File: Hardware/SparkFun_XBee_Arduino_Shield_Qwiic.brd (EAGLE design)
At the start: 53.3 x 59.7 mm, 172 parts, among them J4 QWIIC_RIGHT_ANGLE, Q1 3.1A/30V/105mΩ, Q2 3.1A/30V/105mΩ, Q3 3.1A/30V/105mΩ, Q4 5.8A/30V/35mΩ, Q5 20V/4.2A/52mΩ/1.4W, U1 FSUSB30MUX_MSOP10, U2 AP63203, U3 ESD Diode, U4 FT231XS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

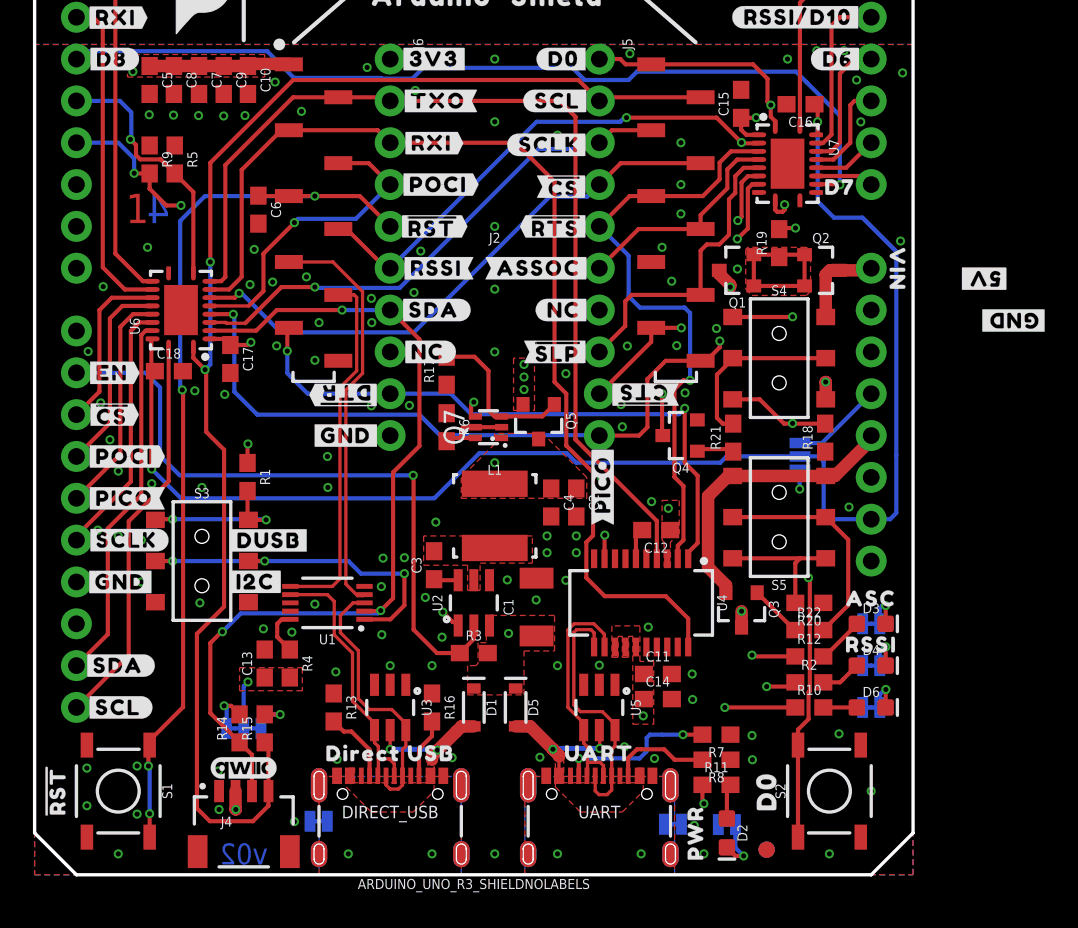
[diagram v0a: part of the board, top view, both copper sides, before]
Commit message: Adds silk
* Adds enable net, needs route
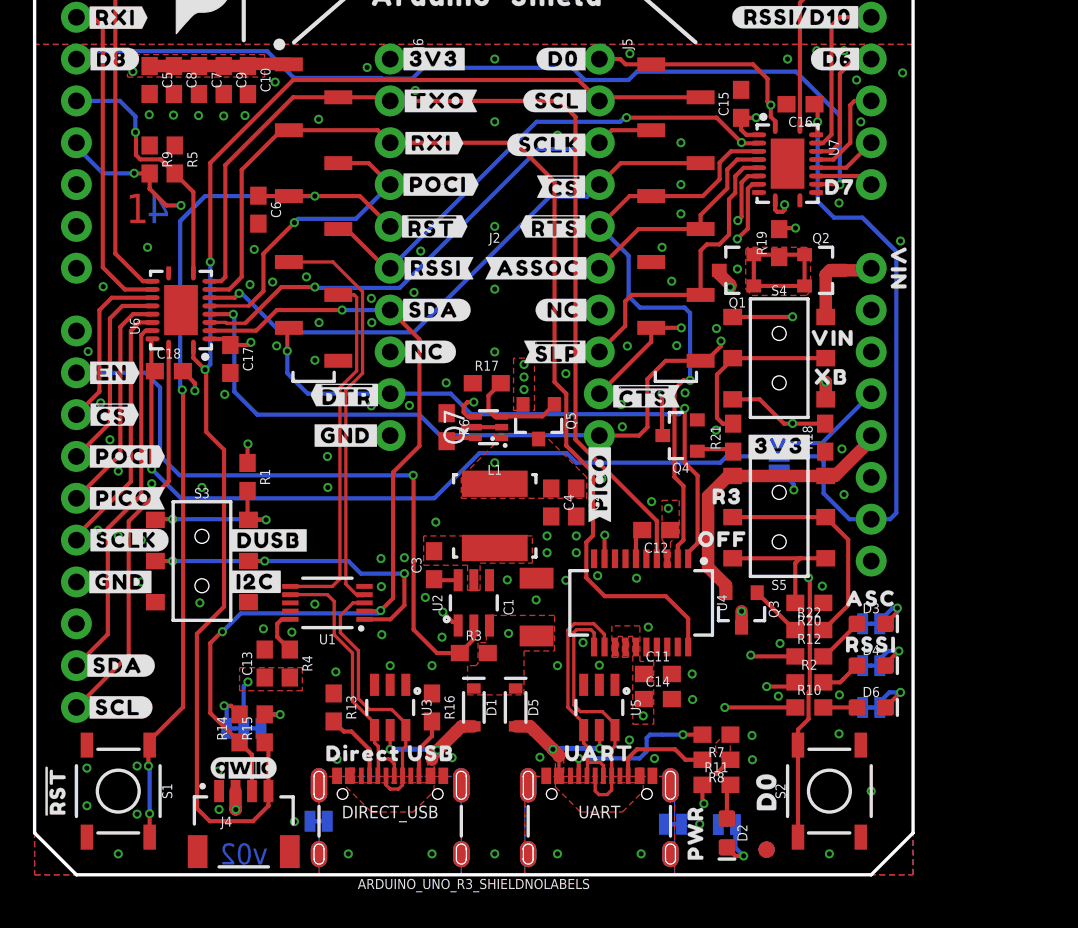
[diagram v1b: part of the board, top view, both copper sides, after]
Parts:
- added U$12: (no value), top:##CTS##28
- added U$41: (no value), topmirror:#GND#0
- added U$44: (no value), top:#3V3#1
- added U$8: (no value), topmirror:##DTR##27
- added U$87: (no value), pot:XB9
- U$31: device topmirror:##CTS##26 -> top:#PICO#26
- U$67: device topmirror:#3V3#2 -> pot:R310
- U$69: device top:##DTR##27 -> pot:OFF311
- U$70: device top:#PICO#24 -> pot:VIN8
- moved U$69 24.5 mm to (41.8, 20.4), turned to 0 degrees
- moved U$70 16.6 mm to (48.5, 32.6), turned to 0 degrees
- moved U$67 16.4 mm to (42.1, 23.0), flipped to the top, turned to 0 degrees
- moved U$29 11.5 mm to (48.1, 31.7), flipped to the bottom, turned to 0 degrees
- moved U$39 11.4 mm to (48.6, 29.2), flipped to the bottom, turned to 0 degrees
- moved U$31 5.92 mm to (34.3, 23.9), turned to 90 degrees
- moved R17 2.55 mm to (27.5, 29.8), turned to 0 degrees
- moved U$89 2.40 mm to (47.0, 25.5)
- moved JP3 1.27 mm to (45.2, 25.4)
- moved U$66 0.08 mm to (52.5, 36.8)
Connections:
- net N$16 renamed OFF_3V3
- net N$24 renamed OFF_VIN
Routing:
- net N$20: track 9.76 -> 6.41 mm
- net GND: track 1.90 -> 4.61 mm, vias 113 -> 123
- net 5V: track 5.56 -> 6.83 mm
- net 3.3V: track 23.9 -> 25.0 mm
- net 3.3V_VREG: track 11.8 -> 12.7 mm
- net N$17: track 2.38 -> 3.12 mm
- net VIN: track 40.0 -> 39.3 mm
- net IOREF: track 87.8 -> 87.3 mm
- net D8/!DTR!: track 54.1 -> 53.6 mm

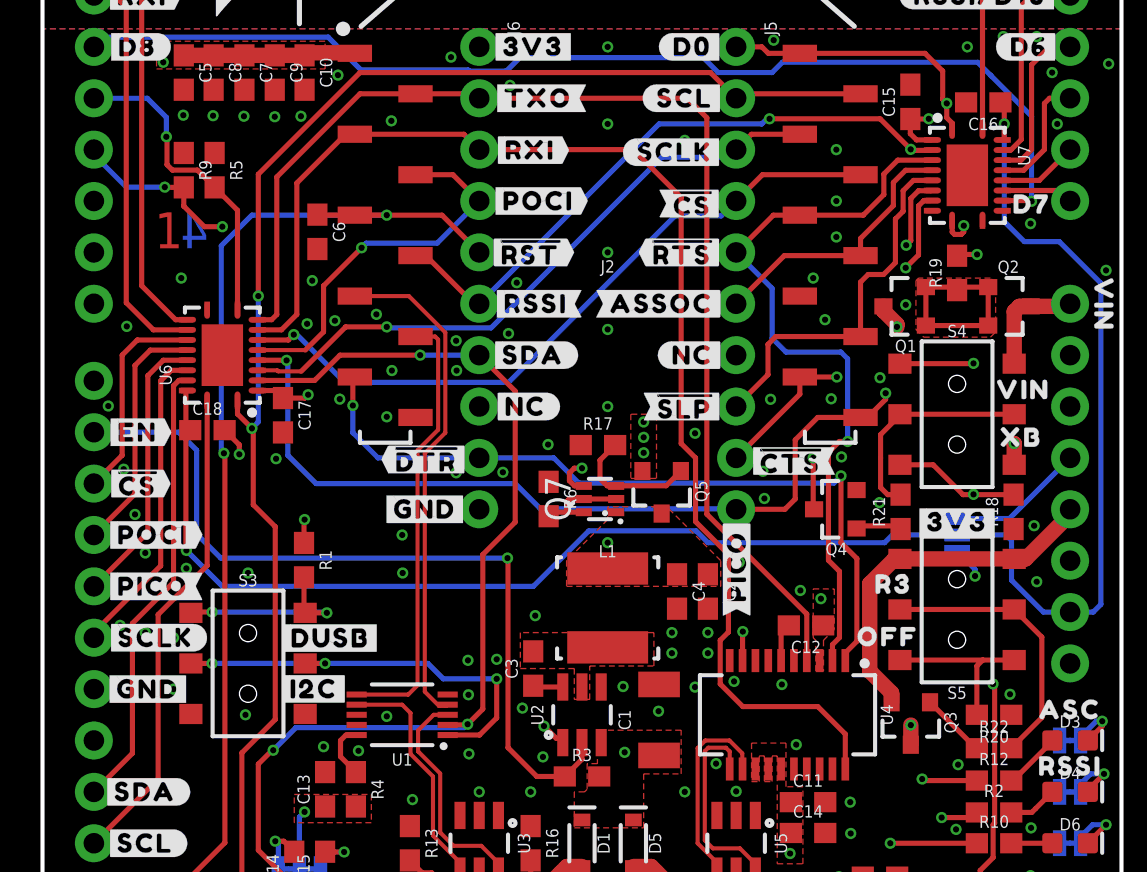
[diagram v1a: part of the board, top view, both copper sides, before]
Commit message: Routes enable pin
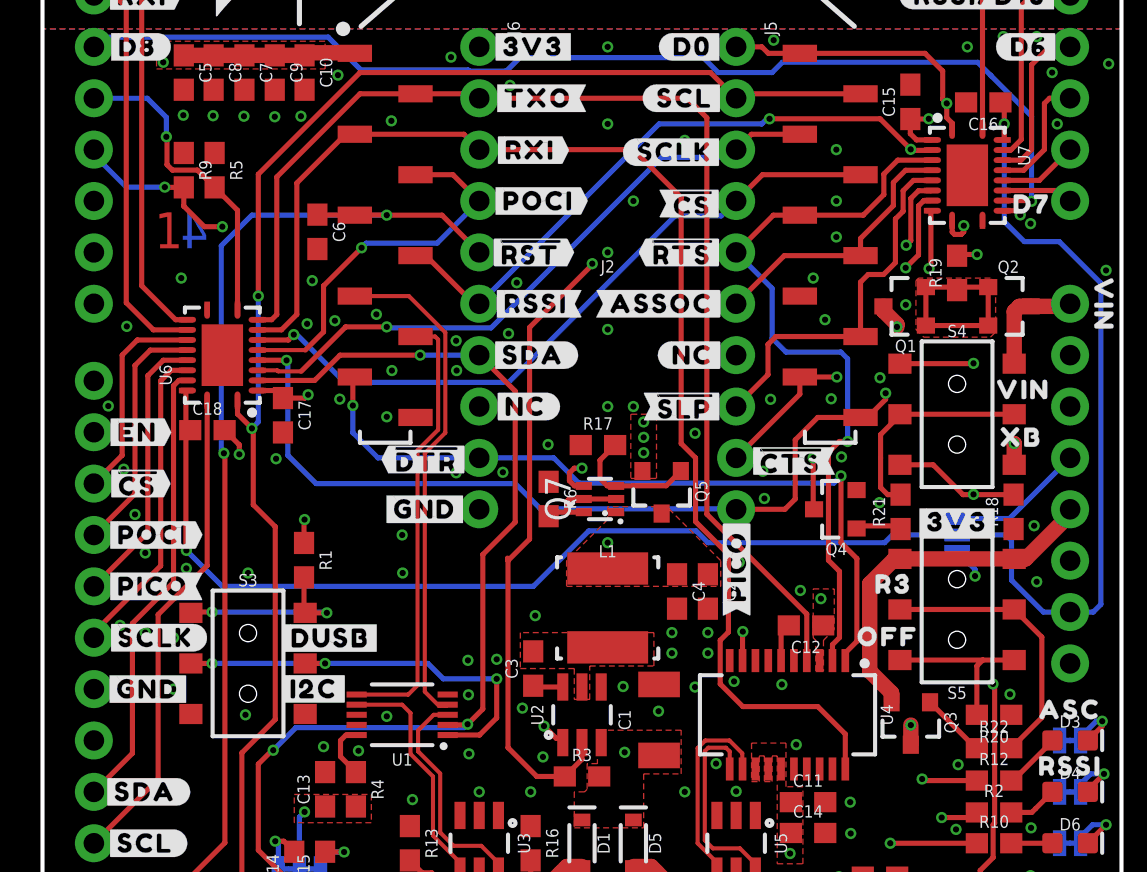
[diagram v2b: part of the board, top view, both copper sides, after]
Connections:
- new net EN_TRANS: B1.D9, U7.12
- net EN: now also U7.9; no longer B1.D9
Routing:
- net EN_TRANS: track 0.00 -> 57.7 mm, vias 0 -> 3
- net EN: track 40.3 -> 51.3 mm, vias 1 -> 2
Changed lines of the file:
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@@
 <wire x1="26.67" y1="14.312" x2="25.82" y2="13.462" width="0.254" layer="1"/>
 <wire x1="25.82" y1="13.462" x2="24.4348" y2="13.462" width="0.254" layer="1"/>
-<wire x1="23.0124" y1="24.2316" x2="23.0124" y2="14.8844" width="0.254" layer="1"/>
+<wire x1="23.0124" y1="24.2316" x2="23.0124" y2="24.13" width="0.254" layer="1"/>
+<wire x1="23.0124" y1="24.13" x2="23.0124" y2="14.8844" width="0.254" layer="1"/>
 <wire x1="24.4348" y1="13.462" x2="23.0124" y2="14.8844" width="0.254" layer="1"/>
 <wire x1="23.0124" y1="24.2316" x2="22.987" y2="24.257" width="0.254" layer="1"/>
-<via x="22.987" y="24.257" extent="1-16" drill="0.3048"/>
-<wire x1="22.987" y1="24.257" x2="8.8138" y2="24.257" width="0.254" layer="16"/>
-<wire x1="8.8138" y1="24.257" x2="7.62" y2="25.4508" width="0.254" layer="16"/>
-<contactref element="B1" pad="D9"/>
-<wire x1="7.62" y1="25.4508" x2="7.62" y2="29.591" width="0.254" layer="16"/>
-<wire x1="7.62" y1="29.591" x2="6.731" y2="30.48" width="0.254" layer="16"/>
-<wire x1="6.731" y1="30.48" x2="2.54" y2="30.48" width="0.254" layer="16"/>
+<contactref element="U7" pad="9"/>
+<wire x1="23.0124" y1="24.13" x2="24.0792" y2="25.1968" width="0.254" layer="1"/>
+<wire x1="24.0792" y1="35.6616" x2="27.2034" y2="38.7858" width="0.254" layer="1"/>
+<wire x1="27.2034" y1="38.7858" x2="27.178" y2="38.8112" width="0.254" layer="1"/>
+<via x="27.178" y="38.8112" extent="1-16" drill="0.3048"/>
+<wire x1="24.0792" y1="25.1968" x2="24.0792" y2="35.6616" width="0.254" layer="1"/>
+<wire x1="27.178" y1="38.8112" x2="32.5882" y2="38.8112" width="0.254" layer="15"/>
+<wire x1="32.5882" y1="38.8112" x2="33.2486" y2="38.1508" width="0.254" layer="15"/>
+<wire x1="33.2486" y1="38.1508" x2="43.434" y2="38.1508" width="0.254" layer="15"/>
+<wire x1="43.434" y1="38.1508" x2="43.8404" y2="38.5572" width="0.254" layer="15"/>
+<wire x1="43.8404" y1="38.5572" x2="43.8277" y2="38.5699" width="0.254" layer="15"/>
+<via x="43.8277" y="38.5699" extent="1-16" drill="0.3048"/>
+<wire x1="43.92" y1="41.43" x2="43.92" y2="38.6622" width="0.254" layer="1"/>
+<wire x1="43.92" y1="38.6622" x2="43.8277" y2="38.5699" width="0.254" layer="1"/>
 </signal>
 <signal name="N$2">
@@
 <wire x1="50.2666" y1="39.9034" x2="48.5394" y2="39.9034" width="0.254" layer="16"/>
 <wire x1="48.5394" y1="39.9034" x2="47.5454" y2="40.8974" width="0.254" layer="16"/>
-<wire x1="47.5454" y1="40.8974" x2="47.5454" y2="45.72" width="0.254" layer="16"/>
+<wire x1="47.5454" y1="40.8974" x2="47.5454" y2="41.91" width="0.254" layer="16"/>
 <via x="47.5454" y="45.72" extent="1-16" drill="0.3048"/>
+<wire x1="47.5454" y1="41.91" x2="47.5454" y2="45.72" width="0.254" layer="16"/>
 <wire x1="52.324" y1="37.846" x2="50.2666" y2="39.9034" width="0.254" layer="16"/>
 </signal>
@@
 <wire x1="46.146" y1="14.859" x2="43.876" y2="17.129" width="0.254" layer="1"/>
 </signal>
+<signal name="EN_TRANS">
+<contactref element="U7" pad="12"/>
+<contactref element="B1" pad="D9"/>
+<wire x1="2.54" y1="30.48" x2="27.94" y2="30.48" width="0.254" layer="15"/>
+<wire x1="27.94" y1="30.48" x2="29.21" y2="31.75" width="0.254" layer="15"/>
+<via x="29.21" y="31.75" extent="1-16" drill="0.3048"/>
+<wire x1="29.21" y1="31.75" x2="29.21" y2="41.91" width="0.254" layer="2"/>
+<via x="29.21" y="41.91" extent="1-16" drill="0.3048"/>
+<wire x1="29.21" y1="41.91" x2="47.6504" y2="41.91" width="0.254" layer="15"/>
+<wire x1="47.6504" y1="41.91" x2="48.3362" y2="41.2242" width="0.254" layer="15"/>
+<via x="48.3362" y="41.2242" extent="1-16" drill="0.3048"/>
+<wire x1="47.52" y1="41.43" x2="48.1304" y2="41.43" width="0.254" layer="1"/>
+<wire x1="48.1304" y1="41.43" x2="48.3362" y2="41.2242" width="0.254" layer="1"/>
+</signal>
 </signals>

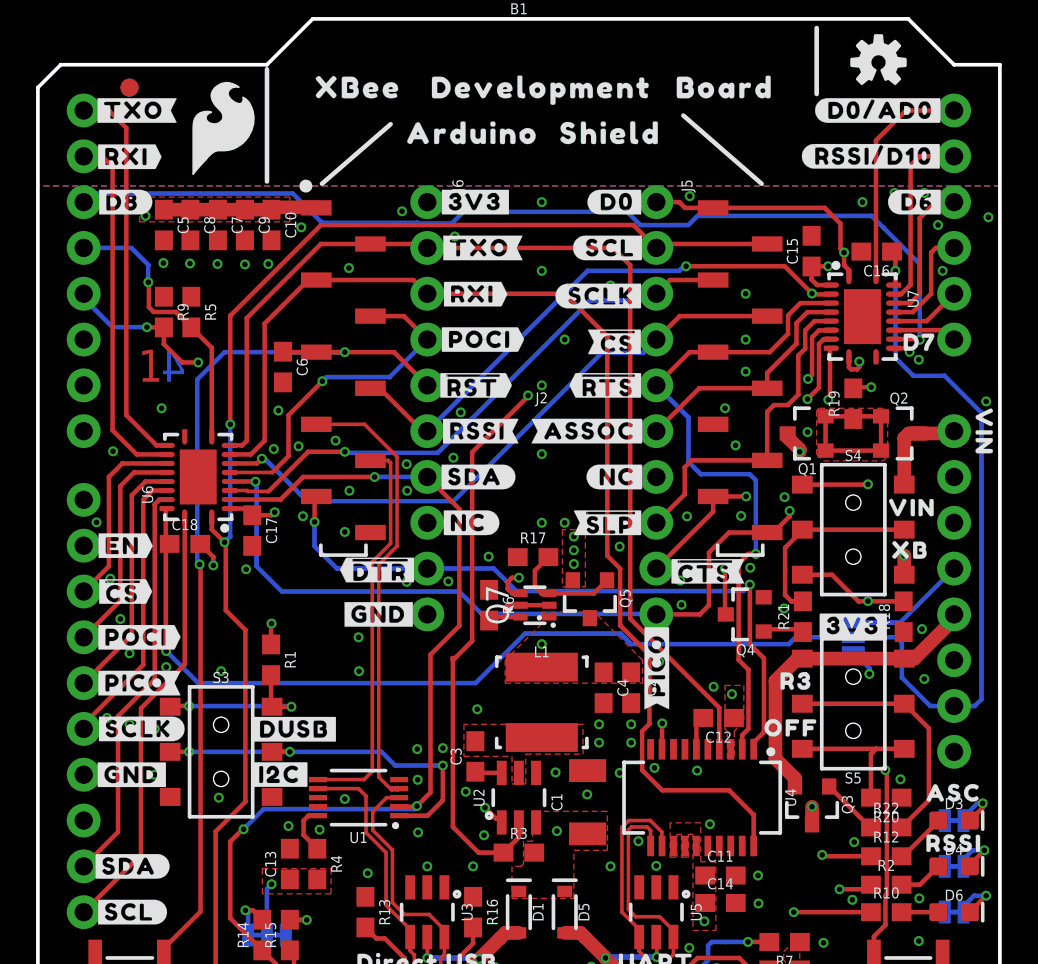
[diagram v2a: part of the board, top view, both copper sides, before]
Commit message: Replaces the PCHAN with a more suitable one
* Routing improvements
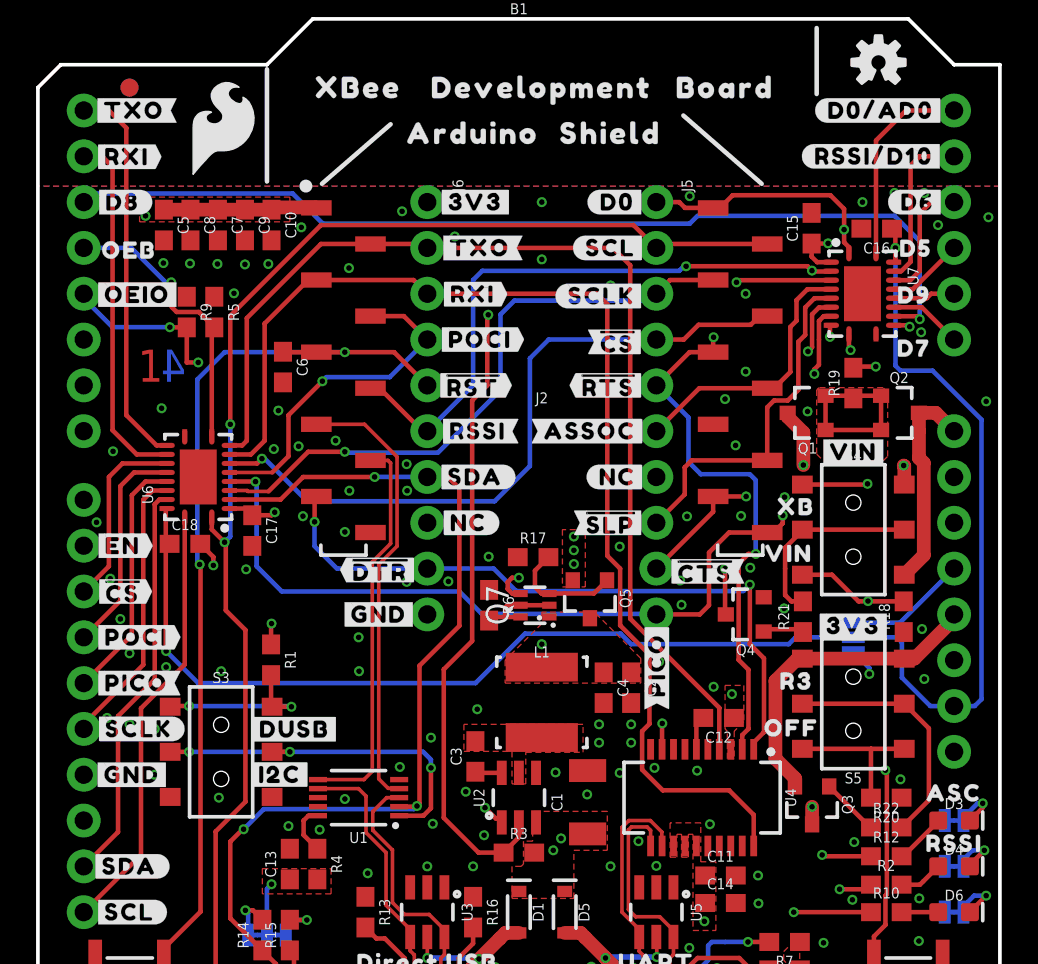
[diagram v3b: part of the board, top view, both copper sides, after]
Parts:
- added U$88: (no value), top:#VIN#4
- added U$90: (no value), pot:#OEIO#59314
- added U$91: (no value), pot:D59313
- added U$92: (no value), pot:D9312
- Q1, Q2: value 3.1A/30V/105mΩ -> 20V/4.2A/52mΩ/1.4W
- R18: value 100k -> 10k
- U$66: device top:VIN5 -> pot:OEB59315
- moved U$66 48.5 mm to (5.05, 46.9), turned to 0 degrees
- moved U$70 7.31 mm to (41.6, 30.0)
- moved U$87 6.79 mm to (42.0, 32.6)
- moved C15 1.27 mm to (42.9, 48.1)
- moved C16 1.27 mm to (46.5, 48.1)
- moved U7 1.27 mm to (45.7, 44.5)
- moved R9 1.27 mm to (8.26, 43.4)
- moved R5 1.27 mm to (9.78, 43.4)
- moved R19 1.14 mm to (45.2, 39.5)
- moved U$42 1.14 mm to (44.6, 38.3)
- moved Q1 1.14 mm to (42.7, 37.8)
- moved Q2 1.14 mm to (47.8, 37.8)
- moved U$83 0.47 mm to (48.6, 41.4)
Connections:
- net OFF_VIN renamed OFF_XB
- net VIN: now also S4.1; no longer S4.3
- net VIN_R3: now also S4.3; no longer S4.1
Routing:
- net VIN_R3: track 5.68 -> 12.1 mm
- net EN: track 51.3 -> 55.6 mm
- net D10/RSSI_PWM: track 67.1 -> 71.2 mm
- net D3/SPI_!CS!: track 35.1 -> 38.6 mm
- net EN_TRANS: track 57.7 -> 54.2 mm, vias 3 -> 1
- net D5/ASSOCIATE: track 48.6 -> 51.7 mm
- net D2/SPI_CLK: track 31.7 -> 34.1 mm
- net D5/ASSOCIATE-TRANS: track 6.09 -> 4.23 mm
- net D6/!RTS!: track 37.2 -> 38.6 mm, vias 1 -> 3
- net IOREF: track 87.3 -> 88.6 mm
- net N$18: track 21.1 -> 22.3 mm
- net D9/!SLEEP!: track 18.6 -> 19.8 mm
- net D10/RSSI_PWM-TRANS: track 10.3 -> 9.05 mm
- net D0-TRANS: track 12.5 -> 11.2 mm
- net D8/!DTR!: track 53.6 -> 54.7 mm
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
